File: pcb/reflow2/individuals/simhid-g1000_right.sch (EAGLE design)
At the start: 73 parts, among them J4 PCB-INTERCONNECT, J5 ZX62-B-5PA(33)-FULL, J6 2212S, SW27 SLLB510100-HS, SW28 TS-1109S-B-B, SW29 TS-1109S-B-B, SW30 TS-1109S-B-B, SW31 TS-1109S-B-B, SW32 TS-1109S-B-B, SW33 TS-1109S-B-B, SW34 TS-1109S-B-B, U4 STM32F411CCU, U5 MCP23S18-E/MJ, U6 MCP1703AT-3302E/CB, X1 16MHz/10pF

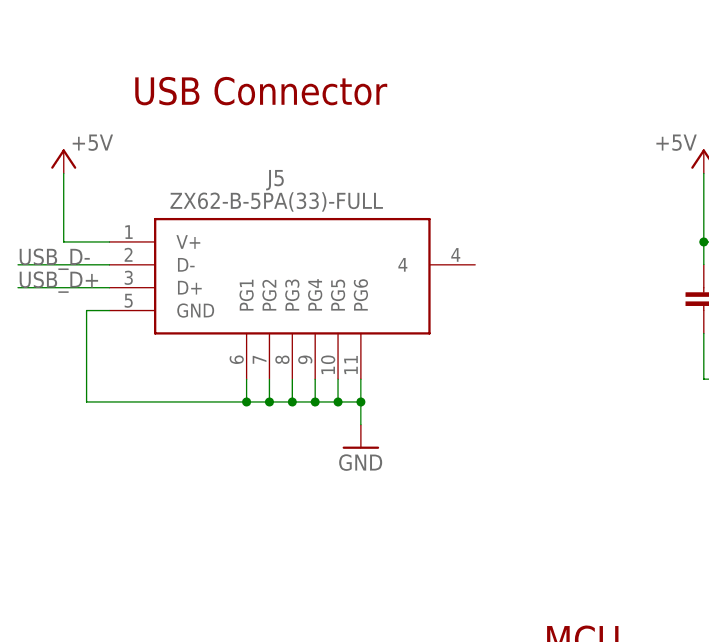
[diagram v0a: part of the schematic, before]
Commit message: Added vertical USB connector versions
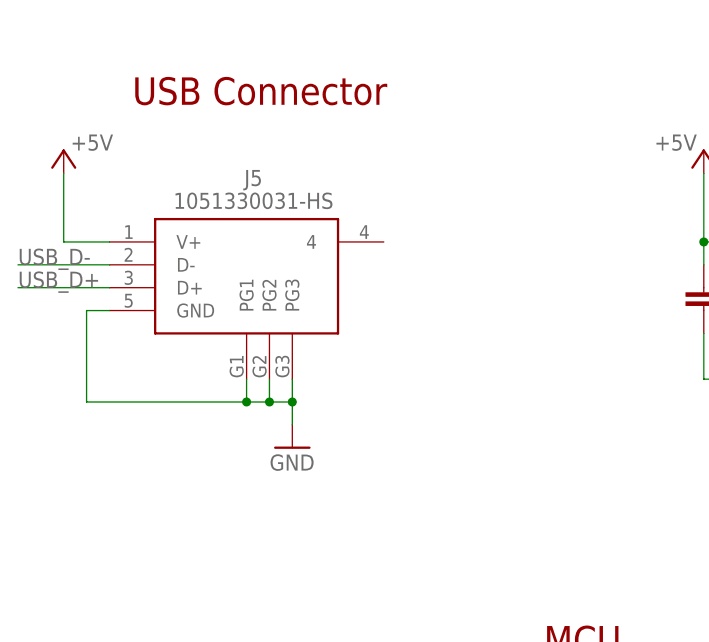
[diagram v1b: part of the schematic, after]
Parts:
- J5: value ZX62-B-5PA(33)-FULL -> 1051330031-HS; device ZX62-B-5PA(33):ZX62-B-5PA(33)-FULL -> USB-connectors:1051330031-HS
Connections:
- net GND: no longer J5.PG4, J5.PG5, J5.PG6
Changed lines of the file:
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@@
 <part name="C15" library="gen-discrete3" library_urn="urn:adsk.eagle:library:8961849" deviceset="RCL_C-EU" device="C0402-HS" package3d_urn="urn:adsk.eagle:package:8961862/3" value="100nF"/>
 <part name="C16" library="gen-discrete3" library_urn="urn:adsk.eagle:library:8961849" deviceset="RCL_C-EU" device="C0402-HS" package3d_urn="urn:adsk.eagle:package:8961862/3" value="4.7uF"/>
-<part name="J5" library="ZX62-B-5PA(33)" library_urn="urn:adsk.eagle:library:5503325" deviceset="ZX62-B-5PA(33)-FULL" device="" package3d_urn="urn:adsk.eagle:package:5503334/4"/>
 <part name="C20" library="gen-discrete3" library_urn="urn:adsk.eagle:library:8961849" deviceset="RCL_C-EU" device="C0402-HS" package3d_urn="urn:adsk.eagle:package:8961862/3" value="100nF"/>
+<part name="J5" library="USB-connectors" library_urn="urn:adsk.eagle:library:41675151" deviceset="1051330031" device="-HS" package3d_urn="urn:adsk.eagle:package:41675482/4"/>
 </parts>
 <sheets>
@@
 <attribute name="VALUE" x="23.622" y="243.84" size="1.778" layer="96" rot="MR0" align="bottom-right"/>
 </instance>
-<instance part="GND1" gate="1" x="55.88" y="210.82" smashed="yes">
-<attribute name="VALUE" x="53.34" y="208.28" size="1.778" layer="96"/>
+<instance part="GND1" gate="1" x="48.26" y="210.82" smashed="yes">
+<attribute name="VALUE" x="45.72" y="208.28" size="1.778" layer="96"/>
 </instance>
 <instance part="U6" gate="G$1" x="147.32" y="210.82" smashed="yes">
@@
 <attribute name="VALUE" x="26.924" y="162.941" size="1.778" layer="96"/>
 </instance>
-<instance part="J5" gate="G$1" x="27.94" y="233.68" smashed="yes">
-<attribute name="NAME" x="46.482" y="240.792" size="1.778" layer="95" align="center"/>
-<attribute name="VALUE" x="46.482" y="238.252" size="1.778" layer="96" align="center"/>
-</instance>
 <instance part="C20" gate="G$1" x="86.36" y="114.3" smashed="yes">
 <attribute name="NAME" x="87.884" y="114.681" size="1.778" layer="95"/>
 <attribute name="VALUE" x="87.884" y="109.601" size="1.778" layer="96"/>
+</instance>
+<instance part="J5" gate="G$1" x="27.94" y="233.68" smashed="yes">
+<attribute name="NAME" x="43.942" y="240.792" size="1.778" layer="95" align="center"/>
+<attribute name="VALUE" x="43.942" y="238.252" size="1.778" layer="96" align="center"/>
 </instance>
 </instances>
@@
 <segment>
 <pinref part="GND1" gate="1" pin="GND"/>
-<wire x1="55.88" y1="218.44" x2="55.88" y2="215.9" width="0.1524" layer="91"/>
-<wire x1="55.88" y1="215.9" x2="55.88" y2="213.36" width="0.1524" layer="91"/>
+<wire x1="48.26" y1="215.9" x2="48.26" y2="213.36" width="0.1524" layer="91"/>
 <wire x1="45.72" y1="218.44" x2="45.72" y2="215.9" width="0.1524" layer="91"/>
 <wire x1="45.72" y1="215.9" x2="48.26" y2="215.9" width="0.1524" layer="91"/>
-<junction x="55.88" y="215.9"/>
-<wire x1="48.26" y1="215.9" x2="50.8" y2="215.9" width="0.1524" layer="91"/>
-<wire x1="50.8" y1="215.9" x2="53.34" y2="215.9" width="0.1524" layer="91"/>
-<wire x1="53.34" y1="215.9" x2="55.88" y2="215.9" width="0.1524" layer="91"/>
 <wire x1="48.26" y1="218.44" x2="48.26" y2="215.9" width="0.1524" layer="91"/>
 <junction x="48.26" y="215.9"/>
-<wire x1="50.8" y1="218.44" x2="50.8" y2="215.9" width="0.1524" layer="91"/>
-<junction x="50.8" y="215.9"/>
-<wire x1="53.34" y1="218.44" x2="53.34" y2="215.9" width="0.1524" layer="91"/>
-<junction x="53.34" y="215.9"/>
-<pinref part="J5" gate="G$1" pin="PG2"/>
-<pinref part="J5" gate="G$1" pin="PG3"/>
-<pinref part="J5" gate="G$1" pin="PG4"/>
-<pinref part="J5" gate="G$1" pin="PG5"/>
-<pinref part="J5" gate="G$1" pin="PG6"/>
 <wire x1="45.72" y1="215.9" x2="43.18" y2="215.9" width="0.1524" layer="91"/>
 <junction x="45.72" y="215.9"/>
-<pinref part="J5" gate="G$1" pin="PG1"/>
 <wire x1="43.18" y1="215.9" x2="43.18" y2="218.44" width="0.1524" layer="91"/>
 <wire x1="43.18" y1="215.9" x2="25.4" y2="215.9" width="0.1524" layer="91"/>
 <junction x="43.18" y="215.9"/>
 <wire x1="25.4" y1="215.9" x2="25.4" y2="226.06" width="0.1524" layer="91"/>
+<wire x1="25.4" y1="226.06" x2="27.94" y2="226.06" width="0.1524" layer="91"/>
 <pinref part="J5" gate="G$1" pin="GND"/>
-<wire x1="25.4" y1="226.06" x2="27.94" y2="226.06" width="0.1524" layer="91"/>
+<pinref part="J5" gate="G$1" pin="PG1"/>
+<pinref part="J5" gate="G$1" pin="PG2"/>
+<pinref part="J5" gate="G$1" pin="PG3"/>
 </segment>
 <segment>
